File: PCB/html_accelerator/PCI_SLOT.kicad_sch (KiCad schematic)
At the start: 13 parts, among them J1 Bus_PCI_Express_x16, J3 PCIexpress_bracket, U1 MCS9990

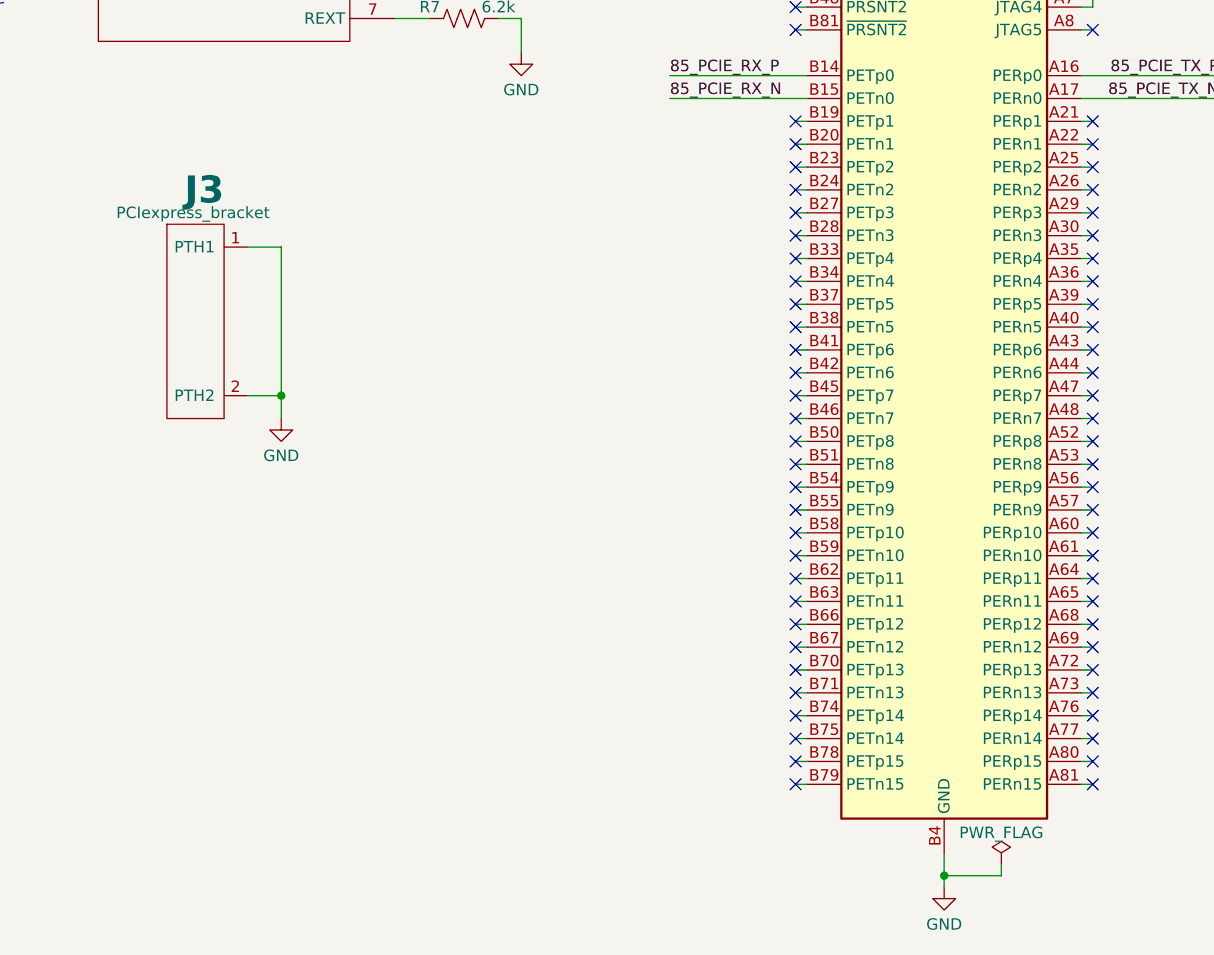
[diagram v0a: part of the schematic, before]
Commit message: constraints for impedance control
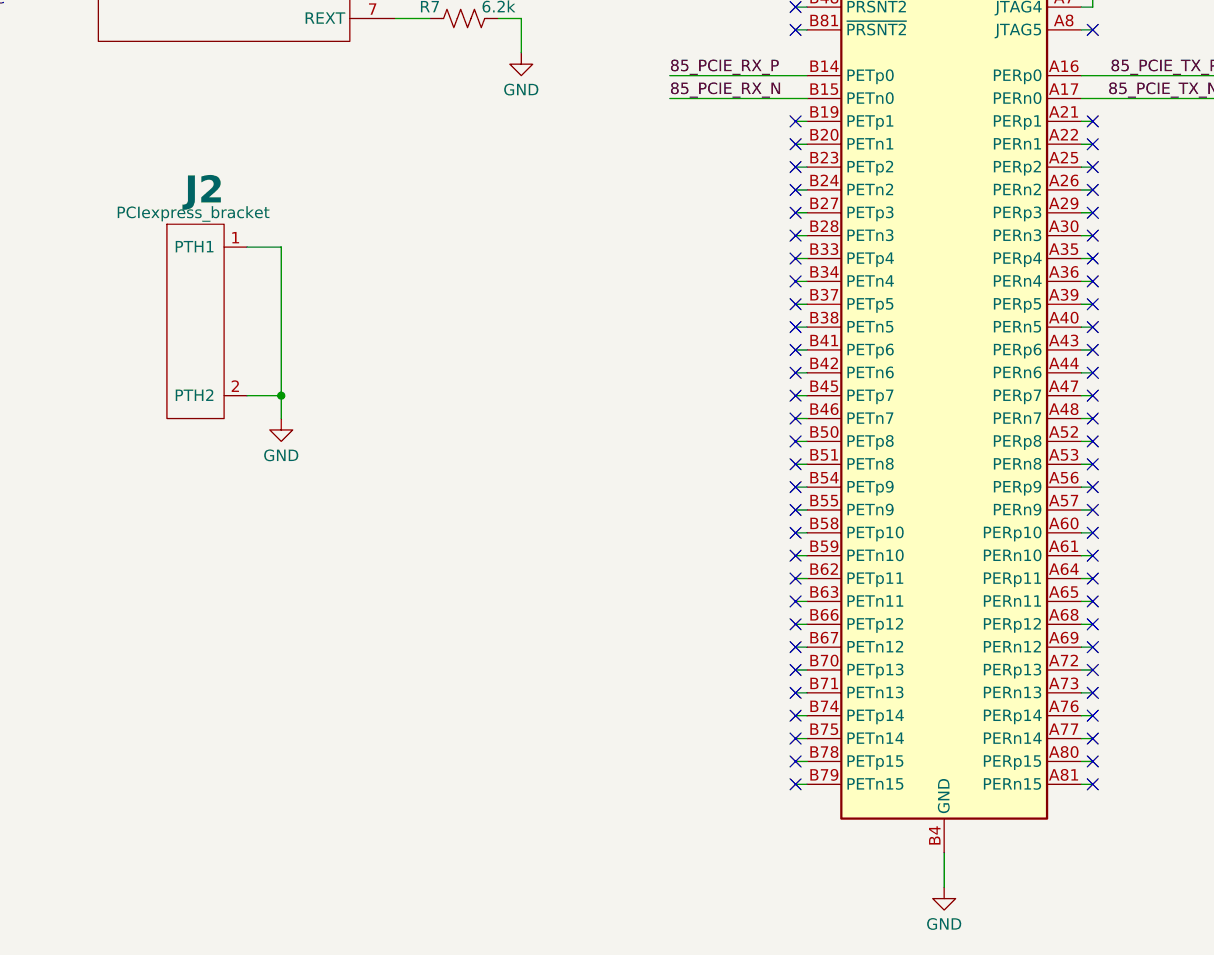
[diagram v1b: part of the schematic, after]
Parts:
- renumbered J3 to J2
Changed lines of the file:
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@@
   (junction (at 111.76 60.96) (diameter 0) (color 0 0 0 0)
-  )
-  (junction (at 152.4 191.77) (diameter 0) (color 0 0 0 0)
   )
   (junction (at 195.58 82.55) (diameter 0) (color 0 0 0 0)
@@
     (stroke (width 0) (type default))
   )
-  (wire (pts (xy 158.75 191.77) (xy 152.4 191.77))
-    (stroke (width 0) (type default))
-  )
   (wire (pts (xy 135.89 125.73) (xy 137.16 125.73))
     (stroke (width 0) (type default))
@@
     (stroke (width 0) (type default))
   )
-  (wire (pts (xy 152.4 189.23) (xy 152.4 191.77))
+  (wire (pts (xy 152.4 189.23) (xy 152.4 193.04))
     (stroke (width 0) (type default))
   )
@@
   )
   (wire (pts (xy 135.89 161.29) (xy 137.16 161.29))
-    (stroke (width 0) (type default))
-  )
-  (wire (pts (xy 158.75 191.77) (xy 158.75 190.5))
-    (stroke (width 0) (type default))
-  )
-  (wire (pts (xy 152.4 193.04) (xy 152.4 191.77))
     (stroke (width 0) (type default))
   )
@@
     )
   )
-  (symbol (lib_id "power:PWR_FLAG") (at 158.75 190.5 0) (unit 1)
-    (in_bom yes) (on_board yes) (dnp no) (fields_autoplaced)
-    (property "Reference" "#FLG01" (at 158.75 188.595 0)
-      (effects (font (size 1.27 1.27)) hide)
-    )
-    (property "Value" "PWR_FLAG" (at 158.75 186.9981 0)
-      (effects (font (size 1.27 1.27)))
-    )
-    (property "Footprint" "" (at 158.75 190.5 0)
-      (effects (font (size 1.27 1.27)) hide)
-    )
-    (property "Datasheet" "~" (at 158.75 190.5 0)
-      (effects (font (size 1.27 1.27)) hide)
-    )
-    (pin "1")
-    (instances
-      (project "html_accelerator"
-        (path "/12b3a7c9-141f-40ba-9ebb-094b58bfa6c7/8c9bd1fc-c6d3-45cd-babe-9d9e8ea6549d"
-          (reference "#FLG01") (unit 1)
-        )
-        (path "/12b3a7c9-141f-40ba-9ebb-094b58bfa6c7/3421334e-11b3-46c8-b0f2-353f0fa6f362"
-          (reference "#FLG010") (unit 1)
-        )
-      )
-    )
-  )
   (symbol (lib_id "power:+3V0") (at 187.96 58.42 0) (unit 1)
     (in_bom yes) (on_board yes) (dnp no) (fields_autoplaced)
@@
   (symbol (lib_id "html_accel_Symbols:PCIexpress_bracket") (at 68.58 129.54 90) (mirror x) (unit 1)
     (in_bom yes) (on_board yes) (dnp no)
-    (property "Reference" "J3" (at 72.39 115.57 90)
+    (property "Reference" "J2" (at 72.39 115.57 90)
       (effects (font (size 3 3) bold) (justify left))
     )
@@
     (instances
       (project "html_accelerator"
-        (path "/12b3a7c9-141f-40ba-9ebb-094b58bfa6c7"
-          (reference "J3") (unit 1)
-        )
         (path "/12b3a7c9-141f-40ba-9ebb-094b58bfa6c7/3421334e-11b3-46c8-b0f2-353f0fa6f362"
           (reference "J2") (unit 1)
@@
   (symbol (lib_id "power:PWR_FLAG") (at 132.08 55.88 0) (unit 1)
     (in_bom yes) (on_board yes) (dnp no) (fields_autoplaced)
-    (property "Reference" "#FLG01" (at 132.08 53.975 0)
+    (property "Reference" "#FLG07" (at 132.08 53.975 0)
       (effects (font (size 1.27 1.27)) hide)
     )
@@
     (instances
       (project "html_accelerator"
-        (path "/12b3a7c9-141f-40ba-9ebb-094b58bfa6c7/8c9bd1fc-c6d3-45cd-babe-9d9e8ea6549d"
-          (reference "#FLG01") (unit 1)
-        )
         (path "/12b3a7c9-141f-40ba-9ebb-094b58bfa6c7/3421334e-11b3-46c8-b0f2-353f0fa6f362"
           (reference "#FLG07") (unit 1)
@@
   (symbol (lib_id "power:PWR_FLAG") (at 118.11 59.69 0) (unit 1)
     (in_bom yes) (on_board yes) (dnp no) (fields_autoplaced)
-    (property "Reference" "#FLG01" (at 118.11 57.785 0)
+    (property "Reference" "#FLG08" (at 118.11 57.785 0)
       (effects (font (size 1.27 1.27)) hide)
     )
@@
     (instances
       (project "html_accelerator"
-        (path "/12b3a7c9-141f-40ba-9ebb-094b58bfa6c7/8c9bd1fc-c6d3-45cd-babe-9d9e8ea6549d"
-          (reference "#FLG01") (unit 1)
-        )
         (path "/12b3a7c9-141f-40ba-9ebb-094b58bfa6c7/3421334e-11b3-46c8-b0f2-353f0fa6f362"
           (reference "#FLG08") (unit 1)
@@
   (symbol (lib_id "power:PWR_FLAG") (at 102.87 60.96 0) (unit 1)
     (in_bom yes) (on_board yes) (dnp no)
-    (property "Reference" "#FLG01" (at 102.87 59.055 0)
+    (property "Reference" "#FLG06" (at 102.87 59.055 0)
       (effects (font (size 1.27 1.27)) hide)
     )
@@
     (instances
       (project "html_accelerator"
-        (path "/12b3a7c9-141f-40ba-9ebb-094b58bfa6c7/8c9bd1fc-c6d3-45cd-babe-9d9e8ea6549d"
-          (reference "#FLG01") (unit 1)
-        )
         (path "/12b3a7c9-141f-40ba-9ebb-094b58bfa6c7/3421334e-11b3-46c8-b0f2-353f0fa6f362"
           (reference "#FLG06") (unit 1)

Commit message: gerbers and readme updates
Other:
- company: (none) -> Spencer K
- title: PCIE Slot, Bracket -> HTML Accelerator
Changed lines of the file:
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@@
 	(paper "A4")
 	(title_block
-		(title "PCIE Slot, Bracket")
-		(date "2024-09-15")
-		(rev "1")
+		(title "HTML Accelerator")
+		(date "2026-04-25")
+		(rev "1.0")
+		(company "Spencer K")
+		(comment 1 "https://github.com/akaStanley/HTML_Accelerator")
 	)
 	(text "85Ω impedance"
